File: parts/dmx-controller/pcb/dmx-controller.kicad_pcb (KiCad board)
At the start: 2 copper layers, 98 x 50 mm, 17 parts, among them J2 PWR IN, SW2 SW_SPDT, U1 ESP32 Wemos D1 Mini

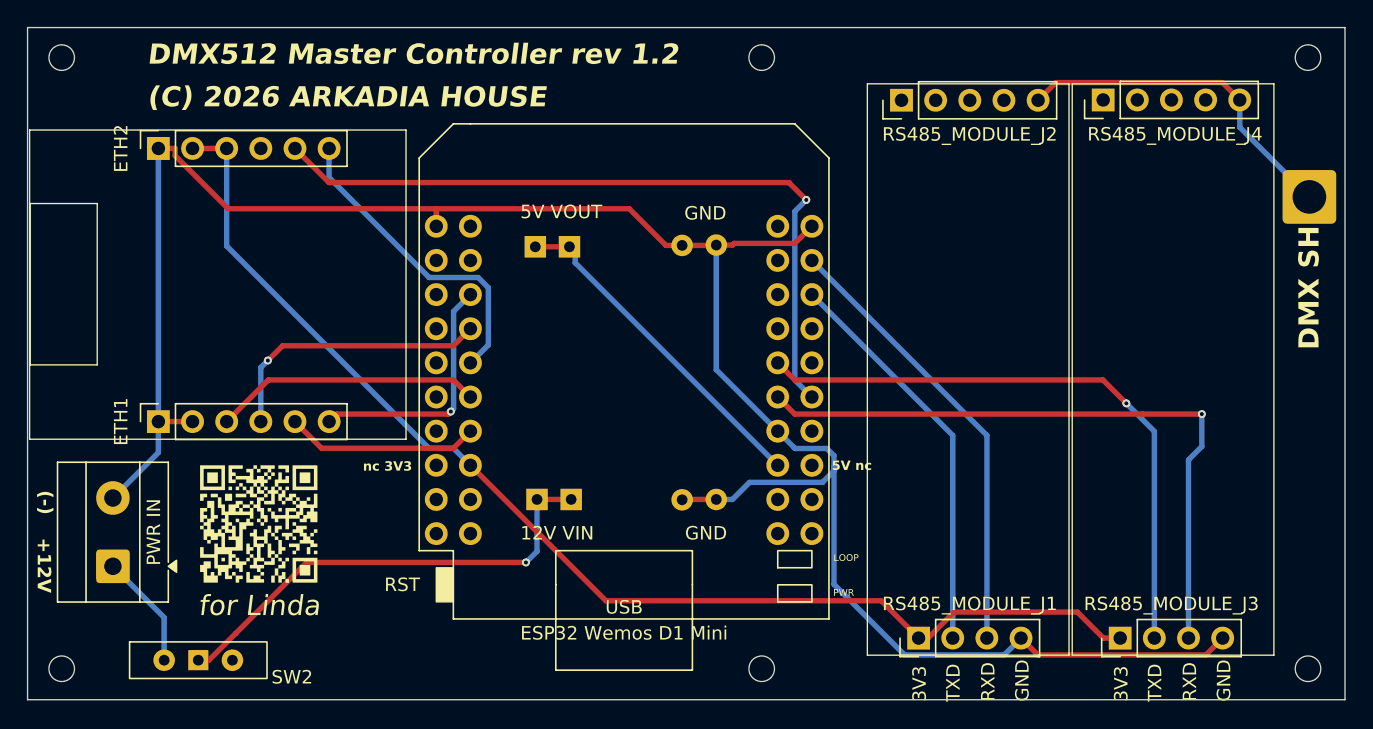
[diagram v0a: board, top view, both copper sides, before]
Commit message: rev the QR code and version of dmx controller pcb
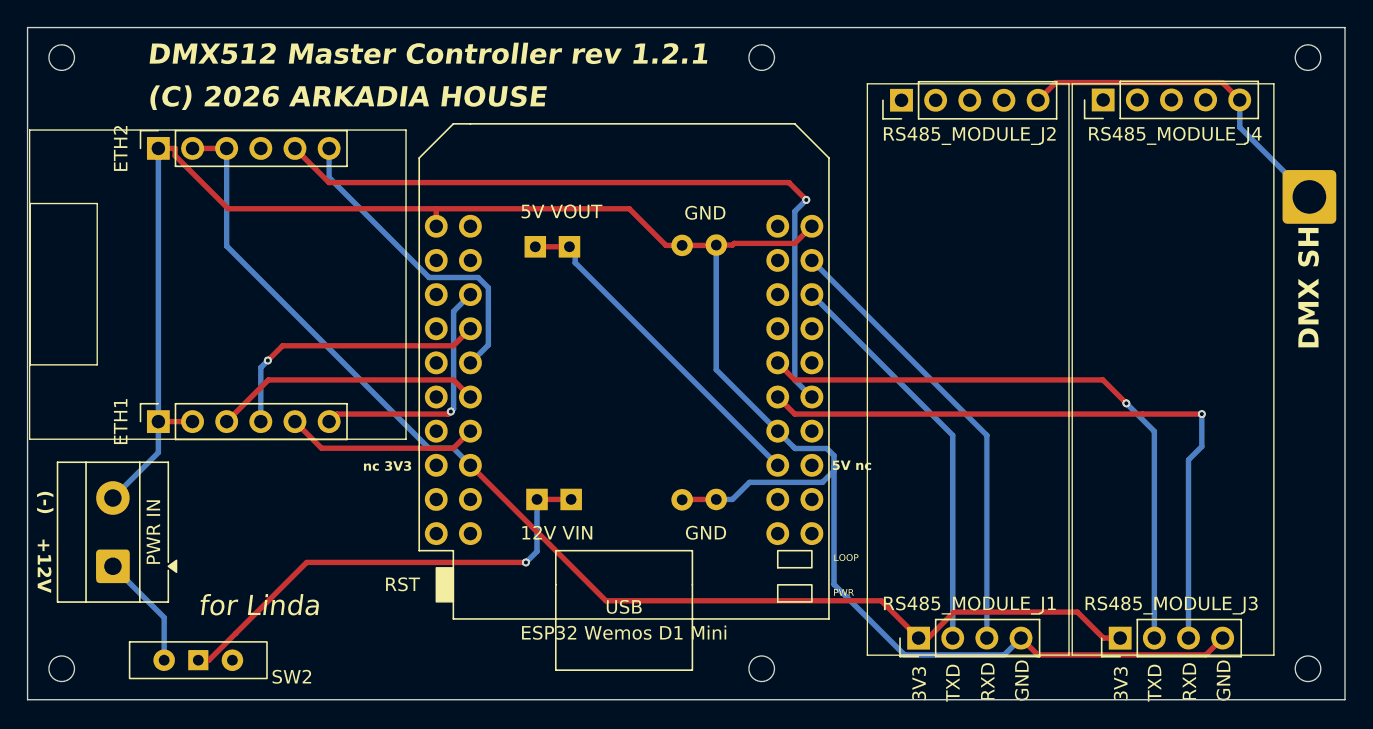
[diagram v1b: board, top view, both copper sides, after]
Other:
- board text added: "DMX512 Master Controller rev 1.2.1"
- board text removed: "DMX512 Master Controller rev 1.2"
